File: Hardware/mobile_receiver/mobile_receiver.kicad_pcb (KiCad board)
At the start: 4 copper layers, 82.5 x 142 mm, 32 parts, among them J1 Conn_02x07_Top_Bottom, SW1 SW_SPST, SW2 SW_Push, SW3 SW_Push, SW4 SW_Push, SW5 SW_Push, SW6 SW_Push, SW7 SW_Push, U2 kb2040

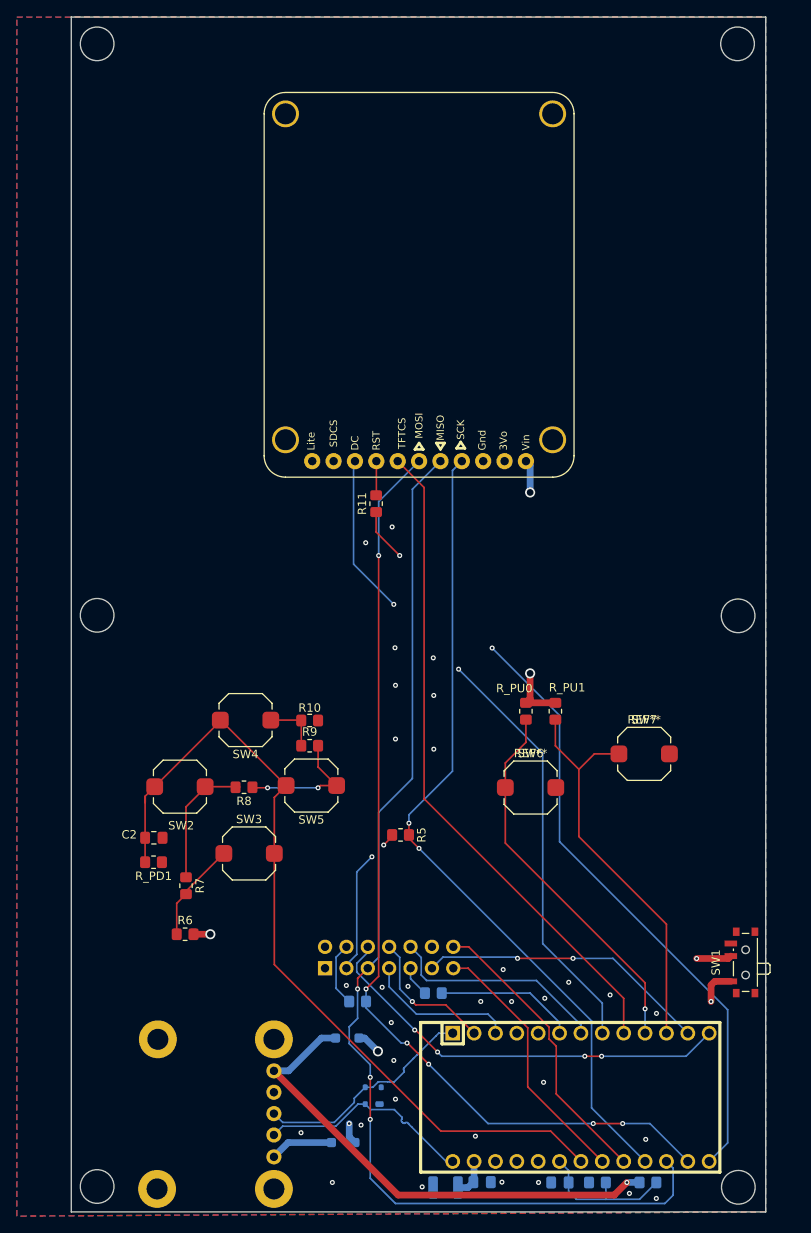
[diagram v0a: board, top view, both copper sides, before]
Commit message: Fixed USB traces, radio connectors, finished UART adapter
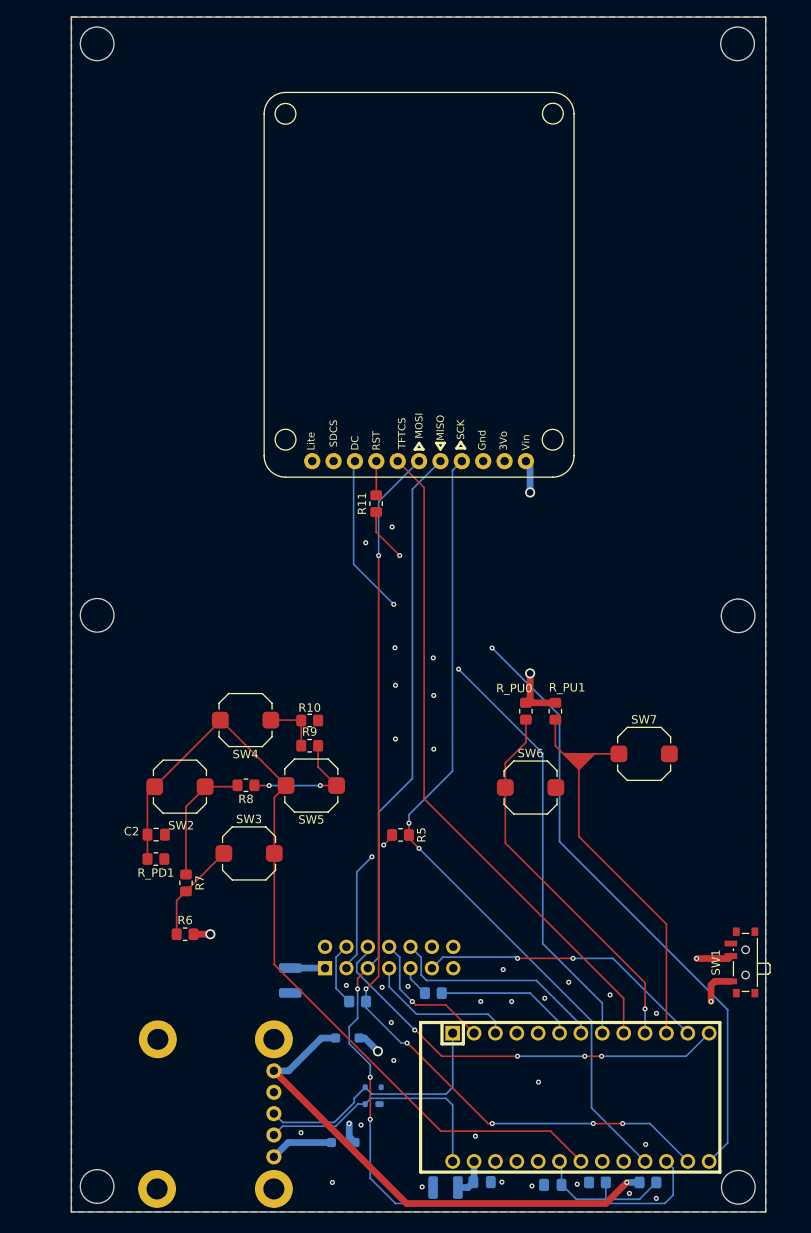
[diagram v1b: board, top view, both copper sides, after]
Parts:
- added C3: 10uF, Capacitor_SMD:C_1210_3225Metric, B.Cu at (192.5, 194.5)
- R4, R5: value 60Ω -> 10K
- moved C1 0.89 mm to (223.7, 218.8)
- moved R_PD1 0.47 mm to (176.5, 180.1)
- moved C2 0.47 mm to (176.6, 177.2)
- moved R7 0.34 mm to (180.1, 182.9)
- moved R8 0.33 mm to (187.2, 171.3)
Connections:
- U2 pad 21: /GPIO1 -> unconnected-(U2-A1/27-Pad21)
- U2 pad 22: /GPIO2 -> unconnected-(U2-A0/26-Pad22)
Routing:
- net /GPIO2: track 35.0 -> 0.00 mm
- net /GPIO1: track 31.3 -> 0.00 mm
- net /USB_DN: track 26.7 -> 30.9 mm
- net /USB_DP: track 26.7 -> 30.8 mm
- net +3.3V: track 144.9 -> 147.4 mm
- net /DPAD_ADC: track 100.8 -> 99.6 mm
- net /VBAT: track 59.1 -> 60.0 mm
- removed copper zone on In1.Cu, net GND
- removed copper zone on In2.Cu, net GND

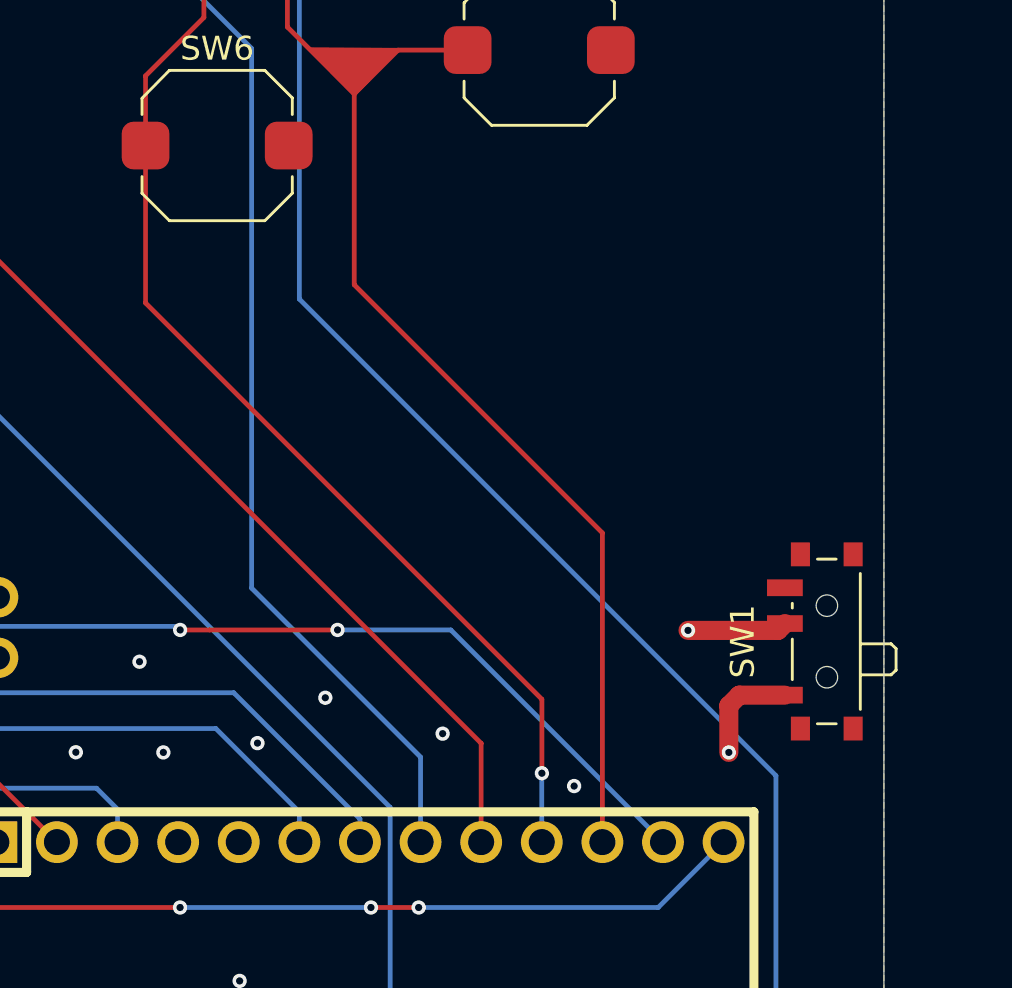
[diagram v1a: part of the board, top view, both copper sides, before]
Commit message: Added new Switch
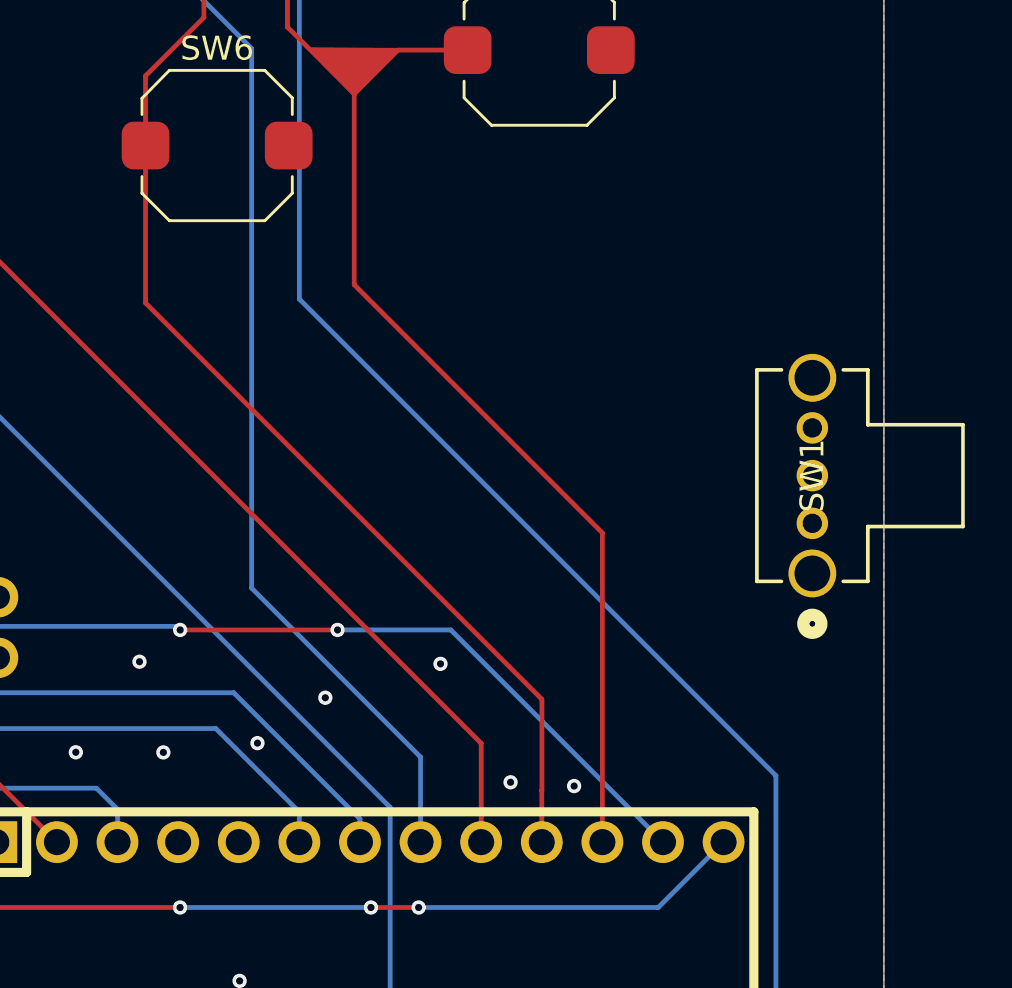
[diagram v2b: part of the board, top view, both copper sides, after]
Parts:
- SW1: footprint Button_Switch_SMD:SW_SPDT_PCM12 -> My footprints:OS102011MA1QN1_CNK
- moved SW1 4.96 mm to (246.0, 187.4)
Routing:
- net /SYS_VBUS: track 56.0 -> 60.1 mm, vias 1 -> 0
- net Net-(D1-K): track 62.1 -> 65.8 mm, vias 3 -> 2
- net /BTN_A: vias 1 -> 0
- net GND: vias 32 -> 33
